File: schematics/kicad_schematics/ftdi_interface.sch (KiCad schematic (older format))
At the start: 9 parts

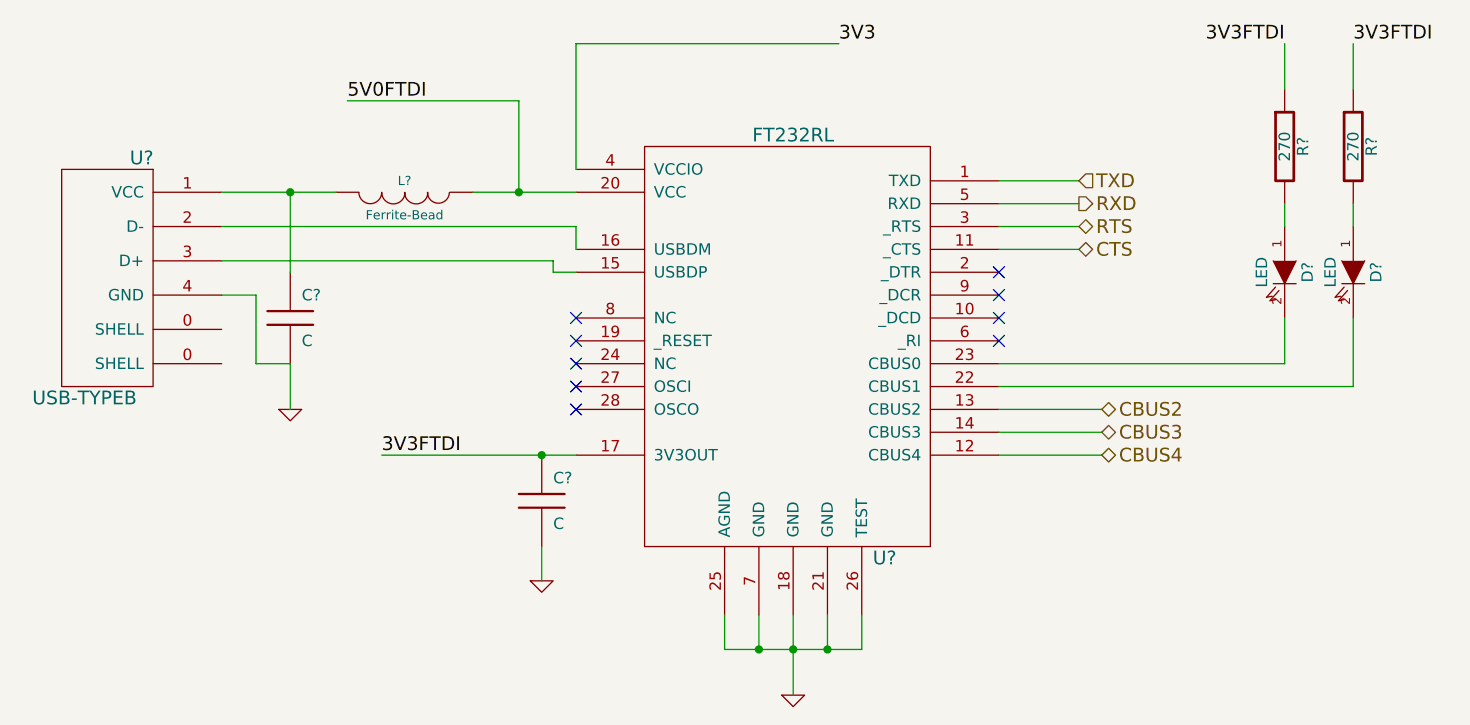
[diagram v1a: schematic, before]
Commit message: Cleaned up Schematic File and modified SD card module, bearboard schematic
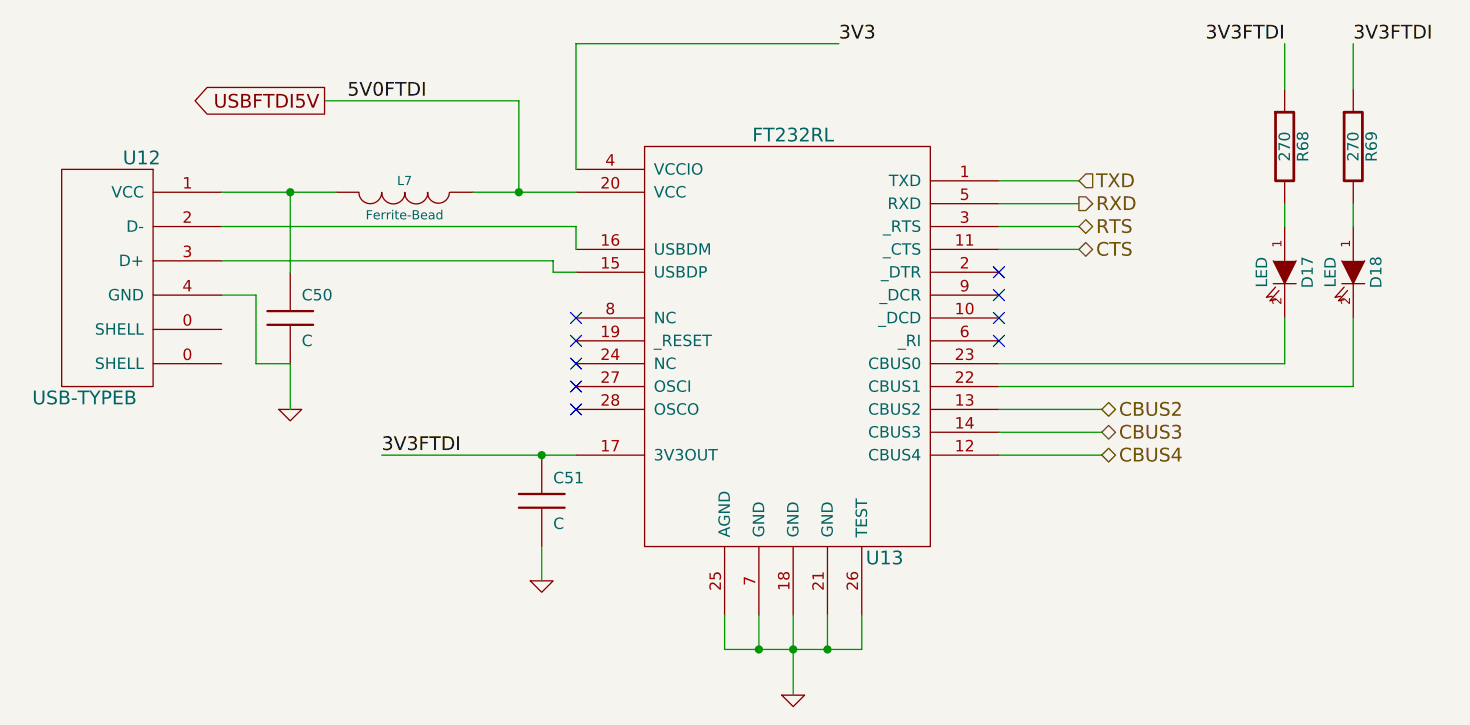
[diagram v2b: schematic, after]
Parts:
- gave numbers to parts that had none: 9
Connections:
- net 5V0FTDI renamed USBFTDI5V
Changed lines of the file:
@@
-EESchema Schematic File Version 2  date Wed 10 Mar 2010 02:43:05 PM EST
+EESchema Schematic File Version 2  date Wed 10 Mar 2010 05:32:05 PM EST
 LIBS:power
 LIBS:device
@@
 Comment4 ""
 $EndDescr
+Wire Wire Line
+	3500 2750 4350 2750
+Wire Wire Line
+	6450 4200 6900 4200
+Wire Wire Line
+	6450 3400 6800 3400
+Wire Wire Line
+	6450 3200 6800 3200
+Wire Wire Line
+	5750 2500 4600 2500
+Wire Wire Line
+	4600 2500 4600 3050
+Connection ~ 4350 3150
+Wire Wire Line
+	4350 2750 4350 3150
+Wire Wire Line
+	7700 3700 7700 3900
+Wire Wire Line
+	7700 3900 6450 3900
+Wire Wire Line
+	7700 2700 7700 2500
+Wire Wire Line
+	7700 3200 7700 3300
+Wire Wire Line
+	3050 3600 3200 3600
+Wire Wire Line
+	3200 3600 3200 3900
+Wire Wire Line
+	3200 3900 3350 3900
+Wire Wire Line
+	5550 5000 5550 5350
+Connection ~ 5550 5150
+Wire Wire Line
+	5850 5000 5850 5150
+Wire Wire Line
+	5850 5150 5250 5150
+Wire Wire Line
+	5250 5150 5250 5000
+Wire Wire Line
+	4600 3400 4600 3300
+Wire Wire Line
+	4600 3300 3050 3300
+Wire Wire Line
+	3550 3150 3050 3150
+Wire Wire Line
+	4150 3150 4600 3150
+Wire Wire Line
+	3050 3450 4500 3450
+Wire Wire Line
+	4500 3450 4500 3500
+Wire Wire Line
+	4500 3500 4600 3500
+Wire Wire Line
+	5400 5000 5400 5150
+Connection ~ 5400 5150
+Wire Wire Line
+	5700 5150 5700 5000
+Connection ~ 5700 5150
+Wire Wire Line
+	3350 3500 3350 3150
+Connection ~ 3350 3150
+Wire Wire Line
+	3350 3900 3350 4100
+Wire Wire Line
+	4450 4700 4450 4850
+Wire Wire Line
+	8000 3200 8000 3300
+Wire Wire Line
+	8000 2700 8000 2500
+Wire Wire Line
+	8000 3700 8000 4000
+Wire Wire Line
+	8000 4000 6450 4000
+Wire Wire Line
+	3750 4300 4600 4300
+Connection ~ 4450 4300
+Wire Wire Line
+	6450 3100 6800 3100
+Wire Wire Line
+	6450 3300 6800 3300
+Wire Wire Line
+	6450 4100 6900 4100
+Wire Wire Line
+	6450 4300 6900 4300
+Text GLabel 3500 2750 0    60   Output ~ 0
+USBFTDI5V
 Text HLabel 6900 4300 2    60   BiDi ~ 0
 CBUS4
@@
 Text HLabel 6900 4100 2    60   BiDi ~ 0
 CBUS2
-Wire Wire Line
-	6450 4300 6900 4300
-Wire Wire Line
-	6450 4100 6900 4100
-Wire Wire Line
-	6450 3300 6800 3300
-Wire Wire Line
-	6450 3100 6800 3100
-Connection ~ 4450 4300
-Wire Wire Line
-	3750 4300 4600 4300
-Wire Wire Line
-	6450 4000 8000 4000
-Wire Wire Line
-	8000 4000 8000 3700
-Wire Wire Line
-	8000 2700 8000 2500
-Wire Wire Line
-	8000 3200 8000 3300
-Wire Wire Line
-	4450 4700 4450 4850
-Wire Wire Line
-	3350 4100 3350 3900
-Connection ~ 3350 3150
-Wire Wire Line
-	3350 3500 3350 3150
-Connection ~ 5700 5150
-Wire Wire Line
-	5700 5150 5700 5000
-Connection ~ 5400 5150
-Wire Wire Line
-	5400 5000 5400 5150
-Wire Wire Line
-	4600 3500 4500 3500
-Wire Wire Line
-	4500 3500 4500 3450
-Wire Wire Line
-	4500 3450 3050 3450
-Wire Wire Line
-	4150 3150 4600 3150
-Wire Wire Line
-	3550 3150 3050 3150
-Wire Wire Line
-	3050 3300 4600 3300
-Wire Wire Line
-	4600 3300 4600 3400
-Wire Wire Line
-	5250 5000 5250 5150
-Wire Wire Line
-	5250 5150 5850 5150
-Wire Wire Line
-	5850 5150 5850 5000
-Connection ~ 5550 5150
-Wire Wire Line
-	5550 5000 5550 5350
-Wire Wire Line
-	3350 3900 3200 3900
-Wire Wire Line
-	3200 3900 3200 3600
-Wire Wire Line
-	3200 3600 3050 3600
-Wire Wire Line
-	7700 3200 7700 3300
-Wire Wire Line
-	7700 2700 7700 2500
-Wire Wire Line
-	6450 3900 7700 3900
-Wire Wire Line
-	7700 3900 7700 3700
-Wire Wire Line
-	4350 3150 4350 2750
-Connection ~ 4350 3150
-Wire Wire Line
-	4350 2750 3600 2750
-Wire Wire Line
-	4600 3050 4600 2500
-Wire Wire Line
-	4600 2500 5750 2500
-Wire Wire Line
-	6450 3200 6800 3200
-Wire Wire Line
-	6450 3400 6800 3400
-Wire Wire Line
-	6450 4200 6900 4200
 Text Label 5750 2500 0    60   ~ 0
 3V3
@@
 5V0FTDI
 $Comp
-L R R?
+L R R69
 U 1 1 4B91C61B
 P 8000 2950
-F 0 "R?" V 8080 2950 50  0000 C CNN
+F 0 "R69" V 8080 2950 50  0000 C CNN
 F 1 "270" V 8000 2950 50  0000 C CNN
 	1    8000 2950
@@
 $EndComp
 $Comp
-L R R?
+L R R68
 U 1 1 4B91C617
 P 7700 2950
-F 0 "R?" V 7780 2950 50  0000 C CNN
+F 0 "R68" V 7780 2950 50  0000 C CNN
 F 1 "270" V 7700 2950 50  0000 C CNN
 	1    7700 2950
@@
 $EndComp
 $Comp
-L LED D?
+L LED D18
 U 1 1 4B91C60D
 P 8000 3500
-F 0 "D?" H 8000 3600 50  0000 C CNN
+F 0 "D18" H 8000 3600 50  0000 C CNN
 F 1 "LED" H 8000 3400 50  0000 C CNN
 	1    8000 3500
@@
 $EndComp
 $Comp
-L LED D?
+L LED D17
 U 1 1 4B91C5FE
 P 7700 3500
-F 0 "D?" H 7700 3600 50  0000 C CNN
+F 0 "D17" H 7700 3600 50  0000 C CNN
 F 1 "LED" H 7700 3400 50  0000 C CNN
 	1    7700 3500
@@
 $EndComp
 $Comp
-L GND #PWR?
+L GND #PWR033
 U 1 1 4B91C5D0
 P 4450 4850
-F 0 "#PWR?" H 4450 4850 30  0001 C CNN
+F 0 "#PWR033" H 4450 4850 30  0001 C CNN
 F 1 "GND" H 4450 4780 30  0001 C CNN
 	1    4450 4850
@@
 $EndComp
 $Comp
-L C C?
+L C C51
 U 1 1 4B91C5C7
 P 4450 4500
-F 0 "C?" H 4500 4600 50  0000 L CNN
+F 0 "C51" H 4500 4600 50  0000 L CNN
 F 1 "C" H 4500 4400 50  0000 L CNN
 	1    4450 4500
@@
 $EndComp
 $Comp
-L GND #PWR?
+L GND #PWR034
 U 1 1 4B91C584
 P 3350 4100
-F 0 "#PWR?" H 3350 4100 30  0001 C CNN
+F 0 "#PWR034" H 3350 4100 30  0001 C CNN
 F 1 "GND" H 3350 4030 30  0001 C CNN
 	1    3350 4100
@@
 $EndComp
 $Comp
-L C C?
+L C C50
 U 1 1 4B91C563
 P 3350 3700
-F 0 "C?" H 3400 3800 50  0000 L CNN
+F 0 "C50" H 3400 3800 50  0000 L CNN
 F 1 "C" H 3400 3600 50  0000 L CNN
 	1    3350 3700
@@
 $EndComp
 $Comp
-L GND #PWR?
+L GND #PWR035
 U 1 1 4B91C510
 P 5550 5350
-F 0 "#PWR?" H 5550 5350 30  0001 C CNN
+F 0 "#PWR035" H 5550 5350 30  0001 C CNN
 F 1 "GND" H 5550 5280 30  0001 C CNN
 	1    5550 5350
@@
 $EndComp
 $Comp
-L INDUCTOR L?
+L INDUCTOR L7
 U 1 1 4B91C4C6
 P 3850 3150
-F 0 "L?" V 3800 3150 40  0000 C CNN
+F 0 "L7" V 3800 3150 40  0000 C CNN
 F 1 "Ferrite-Bead" V 3950 3150 40  0000 C CNN
 	1    3850 3150
@@
 $EndComp
 $Comp
-L USB-TYPEB U?
+L USB-TYPEB U12
 U 1 1 4B91C490
 P 2650 3450
-F 0 "U?" H 2600 3900 60  0000 C CNN
+F 0 "U12" H 2600 3900 60  0000 C CNN
 F 1 "USB-TYPEB" H 2850 2850 60  0000 C CNN
 	1    2650 3450
@@
 $EndComp
 $Comp
-L FT232RL U?
+L FT232RL U13
 U 1 1 4B91C23D
 P 5550 3800
-F 0 "U?" H 5950 2850 60  0000 C CNN
+F 0 "U13" H 5950 2850 60  0000 C CNN
 F 1 "FT232RL" H 5550 4700 60  0000 C CNN
 	1    5550 3800

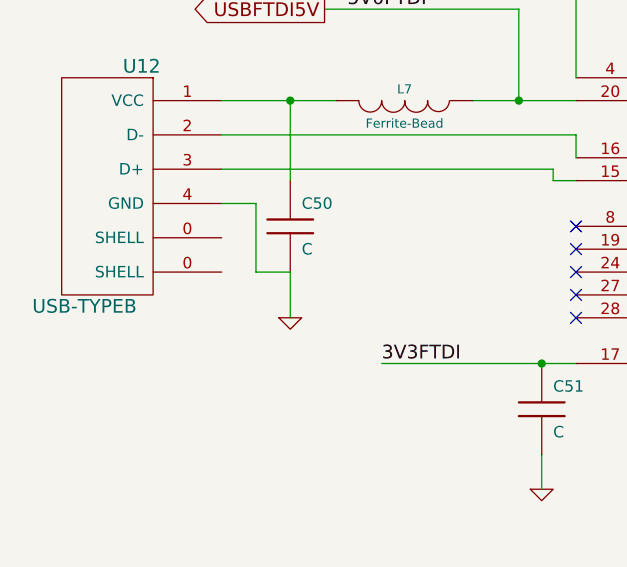
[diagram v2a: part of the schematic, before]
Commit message: Updated USB connector to change the sheild pin to power input Updated the schematic to fix some schematic electrical issues
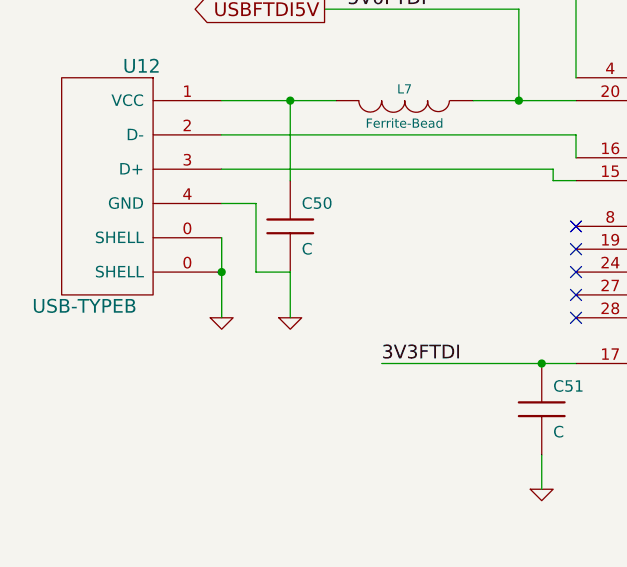
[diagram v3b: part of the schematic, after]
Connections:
- net GND: now also U12.0 (SHELL)
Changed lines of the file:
@@
-EESchema Schematic File Version 2  date Wed 10 Mar 2010 05:32:05 PM EST
+EESchema Schematic File Version 2  date Wed 10 Mar 2010 08:20:30 PM EST
 LIBS:power
 LIBS:device
@@
 Sheet 2 5
 Title ""
-Date "10 mar 2010"
+Date "11 mar 2010"
 Rev ""
 Comp ""
@@
 Comment4 ""
 $EndDescr
+$Comp
+L GND #PWR033
+U 1 1 4B9840B6
+P 3050 4100
+F 0 "#PWR033" H 3050 4100 30  0001 C CNN
+F 1 "GND" H 3050 4030 30  0001 C CNN
+	1    3050 4100
+	1    0    0    -1
+$EndComp
+Connection ~ 3050 3900
+Wire Wire Line
+	3050 4100 3050 3750
 Wire Wire Line
 	3500 2750 4350 2750
@@
 $EndComp
 $Comp
-L GND #PWR033
+L GND #PWR034
 U 1 1 4B91C5D0
 P 4450 4850
-F 0 "#PWR033" H 4450 4850 30  0001 C CNN
+F 0 "#PWR034" H 4450 4850 30  0001 C CNN
 F 1 "GND" H 4450 4780 30  0001 C CNN
 	1    4450 4850
@@
 $EndComp
 $Comp
-L GND #PWR034
+L GND #PWR035
 U 1 1 4B91C584
 P 3350 4100
-F 0 "#PWR034" H 3350 4100 30  0001 C CNN
+F 0 "#PWR035" H 3350 4100 30  0001 C CNN
 F 1 "GND" H 3350 4030 30  0001 C CNN
 	1    3350 4100
@@
 $EndComp
 $Comp
-L GND #PWR035
+L GND #PWR036
 U 1 1 4B91C510
 P 5550 5350
-F 0 "#PWR035" H 5550 5350 30  0001 C CNN
+F 0 "#PWR036" H 5550 5350 30  0001 C CNN
 F 1 "GND" H 5550 5280 30  0001 C CNN
 	1    5550 5350

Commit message: back annotated footprints into eeschem schematic
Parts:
- C50, C51, R68, R69: footprint (none) -> SM0805
- D17, D18: footprint (none) -> LED-0805
- U12: footprint (none) -> mini-usb-b
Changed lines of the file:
@@
-EESchema Schematic File Version 2  date Wed 10 Mar 2010 08:20:30 PM EST
+EESchema Schematic File Version 2  date Fri 12 Mar 2010 11:31:07 AM EST
 LIBS:power
 LIBS:device
@@
 F 0 "R69" V 8080 2950 50  0000 C CNN
 F 1 "270" V 8000 2950 50  0000 C CNN
+F 2 "SM0805" H 8000 2950 60  0001 C CNN
 	1    8000 2950
 	1    0    0    -1
@@
 F 0 "R68" V 7780 2950 50  0000 C CNN
 F 1 "270" V 7700 2950 50  0000 C CNN
+F 2 "SM0805" H 7700 2950 60  0001 C CNN
 	1    7700 2950
 	1    0    0    -1
@@
 F 0 "D18" H 8000 3600 50  0000 C CNN
 F 1 "LED" H 8000 3400 50  0000 C CNN
+F 2 "LED-0805" H 8000 3500 60  0001 C CNN
 	1    8000 3500
 	0    1    1    0
@@
 F 0 "D17" H 7700 3600 50  0000 C CNN
 F 1 "LED" H 7700 3400 50  0000 C CNN
+F 2 "LED-0805" H 7700 3500 60  0001 C CNN
 	1    7700 3500
 	0    1    1    0
@@
 F 0 "C51" H 4500 4600 50  0000 L CNN
 F 1 "C" H 4500 4400 50  0000 L CNN
+F 2 "SM0805" H 4450 4500 60  0001 C CNN
 	1    4450 4500
 	1    0    0    -1
@@
 F 0 "C50" H 3400 3800 50  0000 L CNN
 F 1 "C" H 3400 3600 50  0000 L CNN
+F 2 "SM0805" H 3350 3700 60  0001 C CNN
 	1    3350 3700
 	1    0    0    -1
@@
 F 0 "U12" H 2600 3900 60  0000 C CNN
 F 1 "USB-TYPEB" H 2850 2850 60  0000 C CNN
+F 2 "mini-usb-b" H 2650 3450 60  0001 C CNN
 	1    2650 3450
 	-1   0    0    -1

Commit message: added some more data sheets
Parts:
- U13: footprint (none) -> SSOP28
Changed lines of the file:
@@
-EESchema Schematic File Version 2  date Sat 13 Mar 2010 12:50:25 PM EST
+EESchema Schematic File Version 2  date Sat 13 Mar 2010 02:28:46 PM EST
 LIBS:power
 LIBS:device
@@
 $EndDescr
 $Comp
-L GND #PWR033
+L GND #PWR74
 U 1 1 4B9840B6
 P 3050 4100
-F 0 "#PWR033" H 3050 4100 30  0001 C CNN
+F 0 "#PWR74" H 3050 4100 30  0001 C CNN
 F 1 "GND" H 3050 4030 30  0001 C CNN
 	1    3050 4100
@@
 $EndComp
 $Comp
-L GND #PWR034
+L GND #PWR76
 U 1 1 4B91C5D0
 P 4450 4850
-F 0 "#PWR034" H 4450 4850 30  0001 C CNN
+F 0 "#PWR76" H 4450 4850 30  0001 C CNN
 F 1 "GND" H 4450 4780 30  0001 C CNN
 	1    4450 4850
@@
 $EndComp
 $Comp
-L GND #PWR035
+L GND #PWR75
 U 1 1 4B91C584
 P 3350 4100
-F 0 "#PWR035" H 3350 4100 30  0001 C CNN
+F 0 "#PWR75" H 3350 4100 30  0001 C CNN
 F 1 "GND" H 3350 4030 30  0001 C CNN
 	1    3350 4100
@@
 $EndComp
 $Comp
-L GND #PWR036
+L GND #PWR77
 U 1 1 4B91C510
 P 5550 5350
-F 0 "#PWR036" H 5550 5350 30  0001 C CNN
+F 0 "#PWR77" H 5550 5350 30  0001 C CNN
 F 1 "GND" H 5550 5280 30  0001 C CNN
 	1    5550 5350
@@
 F 0 "U13" H 5950 2850 60  0000 C CNN
 F 1 "FT232RL" H 5550 4700 60  0000 C CNN
+F 2 "SSOP28" H 5550 3800 60  0001 C CNN
 	1    5550 3800
 	1    0    0    -1

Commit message: added npn datasheet
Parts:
- L7: footprint (none) -> SM0805
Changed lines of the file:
@@
-EESchema Schematic File Version 2  date Sat 13 Mar 2010 03:45:55 PM EST
+EESchema Schematic File Version 2  date Sat 13 Mar 2010 04:13:45 PM EST
 LIBS:power
 LIBS:device
@@
 F 0 "L7" V 3800 3150 40  0000 C CNN
 F 1 "Ferrite-Bead" V 3950 3150 40  0000 C CNN
+F 2 "SM0805" H 3850 3150 60  0001 C CNN
 	1    3850 3150
 	0    1    1    0
